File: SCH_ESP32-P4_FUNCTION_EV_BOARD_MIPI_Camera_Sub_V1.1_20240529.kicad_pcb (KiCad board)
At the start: 4 copper layers, 32 x 24 mm, 32 parts, among them J1 FPC_15P_R, J2 FPC_24P, Q3 DUAL_NMOS, SW1 NTC013-AT1J-A160T, U1 ME6211C18M5G-N, U2 ME6211C28M5G-N, Y1 24MHz

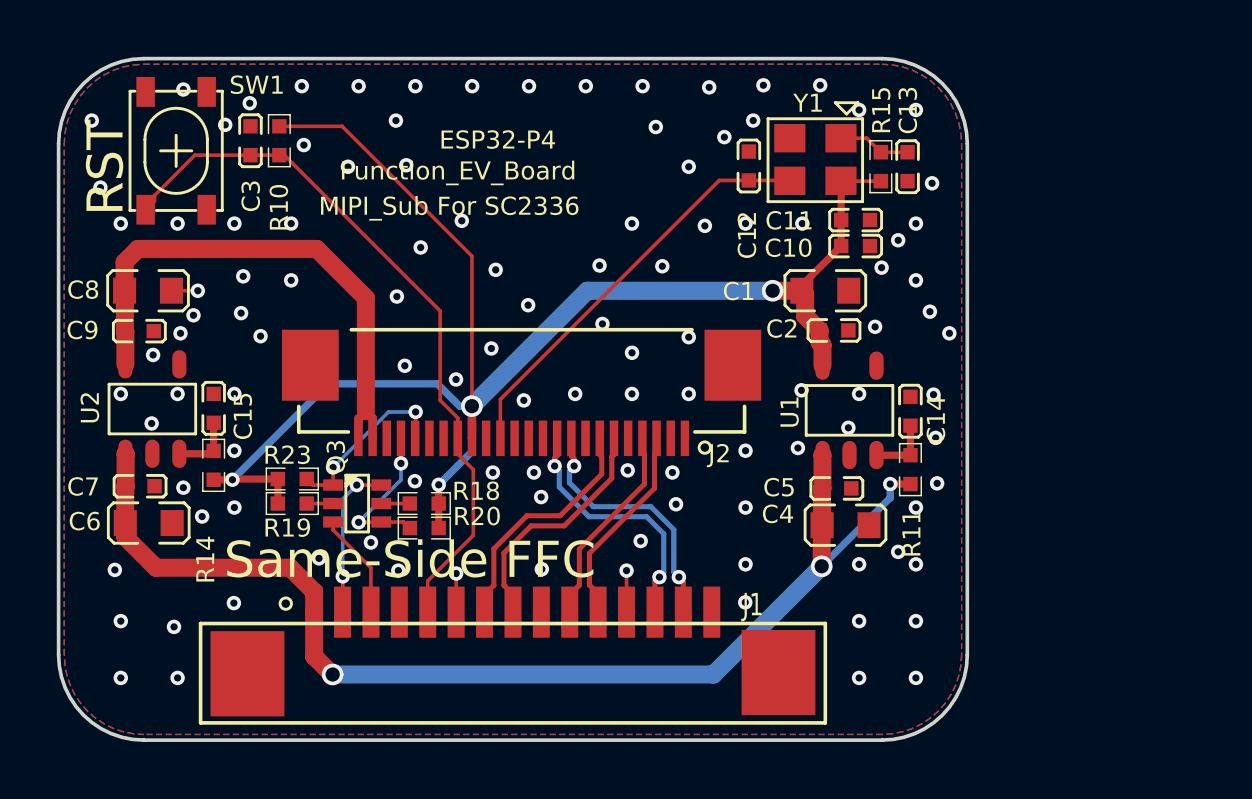
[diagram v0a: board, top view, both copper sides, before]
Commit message: pcb: lay out the SC035HGS adapter board
Update the PCB from the SC035HGS schematic and redo it: all of
Espressif's copper was removed and the parts re-placed and re-routed.
- 40 x 24 mm with R3 corners, 4 layers on JLC04161H-7628, 1.6 mm, ENIG
  (Board Setup minimums from pcb-fabrication-profile.json)
- J1 on the bottom edge, J2 on the top edge, J3 on the right edge
  opening outward (pin row 7.9 mm from the edge, per JAE SJ019575)
- In1 solid GND, In2 solid DOVDD_1V8; 3V3/DVDD_1V5/AVDD_2V8 as tracks
  in PWR_* netclasses
- MIPI CSI-2 pairs on the top layer, 100 ohm (0.2258/0.2032 mm), no
  vias, zero intra-pair skew; all vias 0.6/0.3 mm
- silkscreen text at 1.0/0.15 mm; MECH1/MECH2 dimension holders, the
  Allegro drill chart and off-board empty rule areas removed
- C12/C13/C14 (valued NC) set to DNP in schematic and PCB

DRC: 0 errors, 0 unconnected, 0 schematic parity issues; 86 silkscreen
warnings from Camera_Sub footprints whose silk extends past their
courtyards.

Co-Authored-By: Claude Opus 5.5 <noreply@anthropic.com>
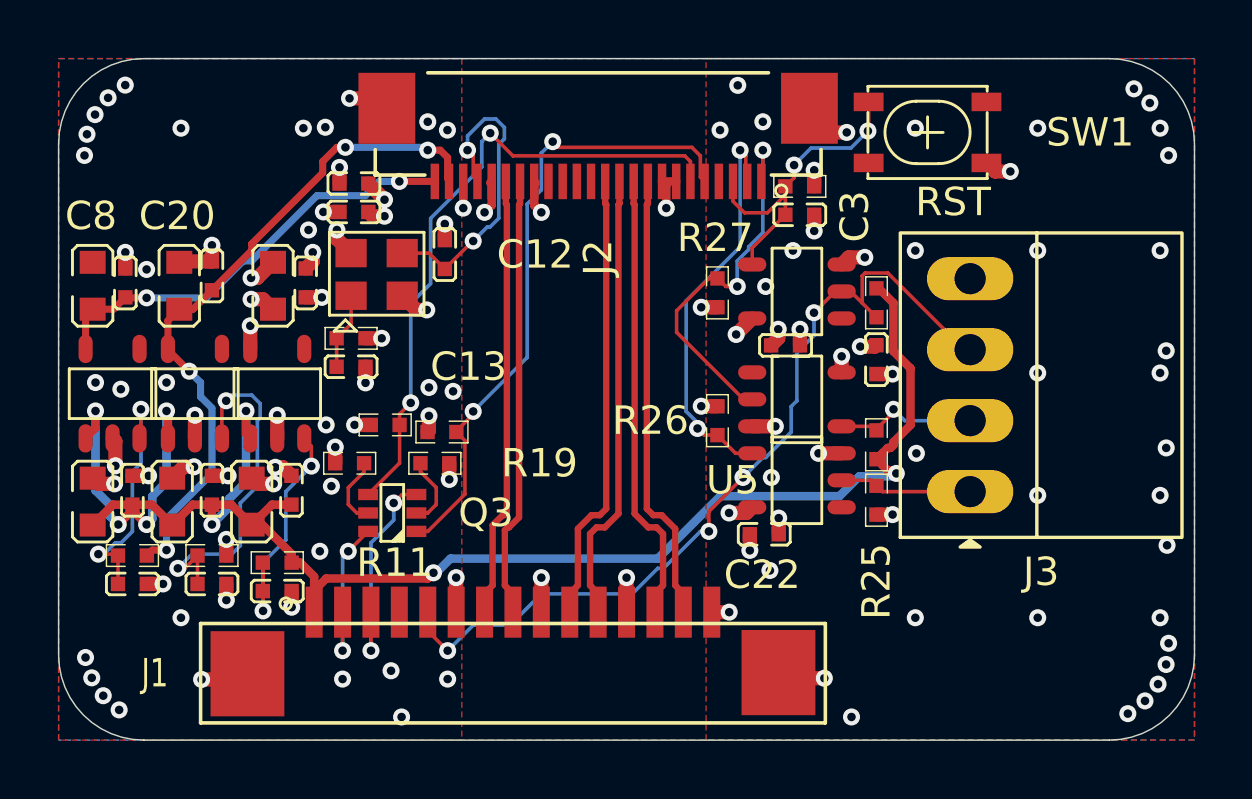
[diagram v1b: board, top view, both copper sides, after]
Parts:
- removed MECH1, MECH2: , 
- added C16: 10uF/6.3V(20%), Camera_Sub:C0603, F.Cu at (4.00, -8.40)
- added C17: 0.1uF/50V(10%), Camera_Sub:C0402, F.Cu at (5.40, -8.80)
- added C18: 0.1uF/50V(10%), Camera_Sub:C0402, F.Cu at (5.40, -5.50)
- added C19: 0.1uF/50V(10%), Camera_Sub:C0402, F.Cu at (5.40, -16.4)
- added C20: 10uF/6.3V(20%), Camera_Sub:C0603, F.Cu at (4.25, -16.0)
- added C21: 0.1uF/50V(10%), Camera_Sub:C0402, F.Cu at (25.6, -13.9)
- added C22: 0.1uF/50V(10%), Camera_Sub:C0402, F.Cu at (24.9, -7.25)
- added C23: 0.1uF/50V(10%), Camera_Sub:C0402, F.Cu at (28.8, -13.4)
- added J3: IL-G-4P-S3L2-SA, SC035HGS_Mod:JAE_IL-G-4P-S3L2-SA_1x04_P2.50mm_Horizontal, F.Cu at (32.1, -12.5)
- added R12: 10K(1%), Camera_Sub:R0402, F.Cu at (5.40, -6.50)
- added R24: 10K(1%), Camera_Sub:R0402, F.Cu at (28.8, -15.4)
- added R25: 100K(1%), Camera_Sub:R0402, F.Cu at (28.8, -8.45)
- added R26: 2.2K(1%), Camera_Sub:R0402, F.Cu at (23.2, -11.2)
- added R27: 100K(1%), Camera_Sub:R0402, F.Cu at (23.2, -15.8)
- added R28: 10K(1%), Camera_Sub:R0402, F.Cu at (28.8, -10.4)
- added U3: ME6211C15M5G-N, Camera_Sub:SOT23-5, F.Cu at (4.80, -12.2)
- added U4: SN74LVC1G07DBVR, Camera_Sub:SOT23-5, F.Cu at (26.0, -15.8)
- added U5: SN74LVC1G07DBVR, Camera_Sub:SOT23-5, F.Cu at (26.0, -9.15)
- added U6: SN74LVC1G07DBVR, Camera_Sub:SOT23-5, F.Cu at (26.0, -12.0)
- moved SW1 26.5 mm to (30.6, -21.4), turned to 180 degrees
- moved C14 23.2 mm to (7.70, -5.25), turned to 0 degrees
- moved R11 22.5 mm to (7.70, -6.25), turned to 0 degrees
- moved C4 20.9 mm to (6.80, -8.40), turned to 90 degrees
- moved C13 20.8 mm to (10.3, -13.2), turned to 0 degrees
- moved U1 20.2 mm to (7.70, -12.2)
- moved R15 19.6 mm to (10.3, -14.2), turned to 0 degrees
- moved C3 19.5 mm to (26.1, -18.5), turned to 0 degrees
- moved C1 19.5 mm to (7.55, -16.0), turned to 90 degrees
- moved C5 19.2 mm to (8.20, -8.80), turned to 90 degrees
- moved C2 18.7 mm to (8.70, -16.1), turned to 90 degrees
- moved R10 18.4 mm to (26.1, -19.5), turned to 0 degrees
- moved C10 17.8 mm to (10.4, -19.6)
- moved C11 17.7 mm to (10.4, -18.6)
- moved Y1 16.0 mm to (11.2, -16.4), turned to 0 degrees
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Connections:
- C12 pad 1: /XVCLK -> /MCLK
- C3 pad 1: /RESET -> /XSHUTDN
- J1 pad 5: /RESET -> /XSHUTDN_3V3
- J2 pad 1: unconnected-(J2-Pad1) -> /LED_STROBE
- J2 pad 11: unconnected-(J2-Pad11) -> /CSI_DATA1N
- J2 pad 12: unconnected-(J2-Pad12) -> /CSI_DATA1P
- J2 pad 13: GND -> unconnected-(J2-NC-Pad13)
- J2 pad 14: /XVCLK -> unconnected-(J2-NC-Pad14)
- J2 pad 15: GND -> unconnected-(J2-NC-Pad15)
- J2 pad 16: DOVDD_1V8 -> unconnected-(J2-NC-Pad16)
- J2 pad 17: /RESET -> GND
- J2 pad 18: unconnected-(J2-Pad18) -> /CSI_CLKN
- J2 pad 19: GND -> /CSI_CLKP
- J2 pad 2: unconnected-(J2-Pad2) -> /TRIG
- J2 pad 20: /SENSOR_SDA -> GND
- J2 pad 21: /SENSOR_SCL -> /MCLK
- J2 pad 22: GND -> DOVDD_1V8
- J2 pad 23: AVDD_2V8 -> DVDD_1V5
- J2 pad 3: /CSI_DATA1N -> /XSHUTDN
- J2 pad 4: /CSI_DATA1P -> unconnected-(J2-NC-Pad4)
- J2 pad 5: GND -> /SENSOR_SDA
- J2 pad 6: /CSI_CLKN -> /SENSOR_SCL
- J2 pad 7: /CSI_CLKP -> GND
- R10 pad 1: /RESET -> /XSHUTDN
- R14 pad 2: DOVDD_1V8 -> DVDD_1V5
- SW1 pad 3: /RESET -> /XSHUTDN
- Y1 pad 3: /XVCLK -> /MCLK
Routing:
- net DOVDD_1V8: track 55.3 -> 14.0 mm, vias 4 -> 21
- net GND: track 3.75 -> 38.2 mm, vias 113 -> 104
- net /XSHUTDN_3V3: track 0.00 -> 30.7 mm, vias 0 -> 4
- net /RESET: track 25.3 -> 0.00 mm
- net DVDD_1V5: track 0.00 -> 23.9 mm, vias 0 -> 4
- net 3V3: track 40.9 -> 61.1 mm, vias 3 -> 8
- net /SENSOR_SCL: track 5.47 -> 22.7 mm
- net /SENSOR_SDA: track 6.29 -> 22.5 mm
- net /XVCLK: track 14.8 -> 0.00 mm
- net /TRIG: track 0.00 -> 14.2 mm, vias 0 -> 2
- net /LED_STROBE: track 0.00 -> 13.4 mm, vias 0 -> 2
- net Net-(U3-EN): track 0.00 -> 12.5 mm, vias 0 -> 2
- net /XSHUTDN: track 0.00 -> 11.2 mm, vias 0 -> 2
- net /MCLK: track 0.00 -> 11.1 mm, vias 0 -> 2
- net /CSI_DATA1N: track 7.23 -> 15.9 mm
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- added copper zone on In2.Cu, net DOVDD_1V8
- removed copper zone on In2.Cu, net GND
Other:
- board size 32 x 24 mm -> 40 x 24 mm
- board text added: "MIPI_Sub For SC035HGS"
- board text removed: "0.254"
- board text removed: "0.5"
- board text removed: "126"
- board text removed: "4"
- board text removed: "ALL UNITS ARE IN MILLIMETERS"
- board text removed: "DRILL CHART: TOP to BOTTOM"
- board text removed: "FIGURE"
- board text removed: "MIPI_Sub For SC2336"
- board text removed: "PLATED"
- board text removed: "QTY"
- board text removed: "SIZE"

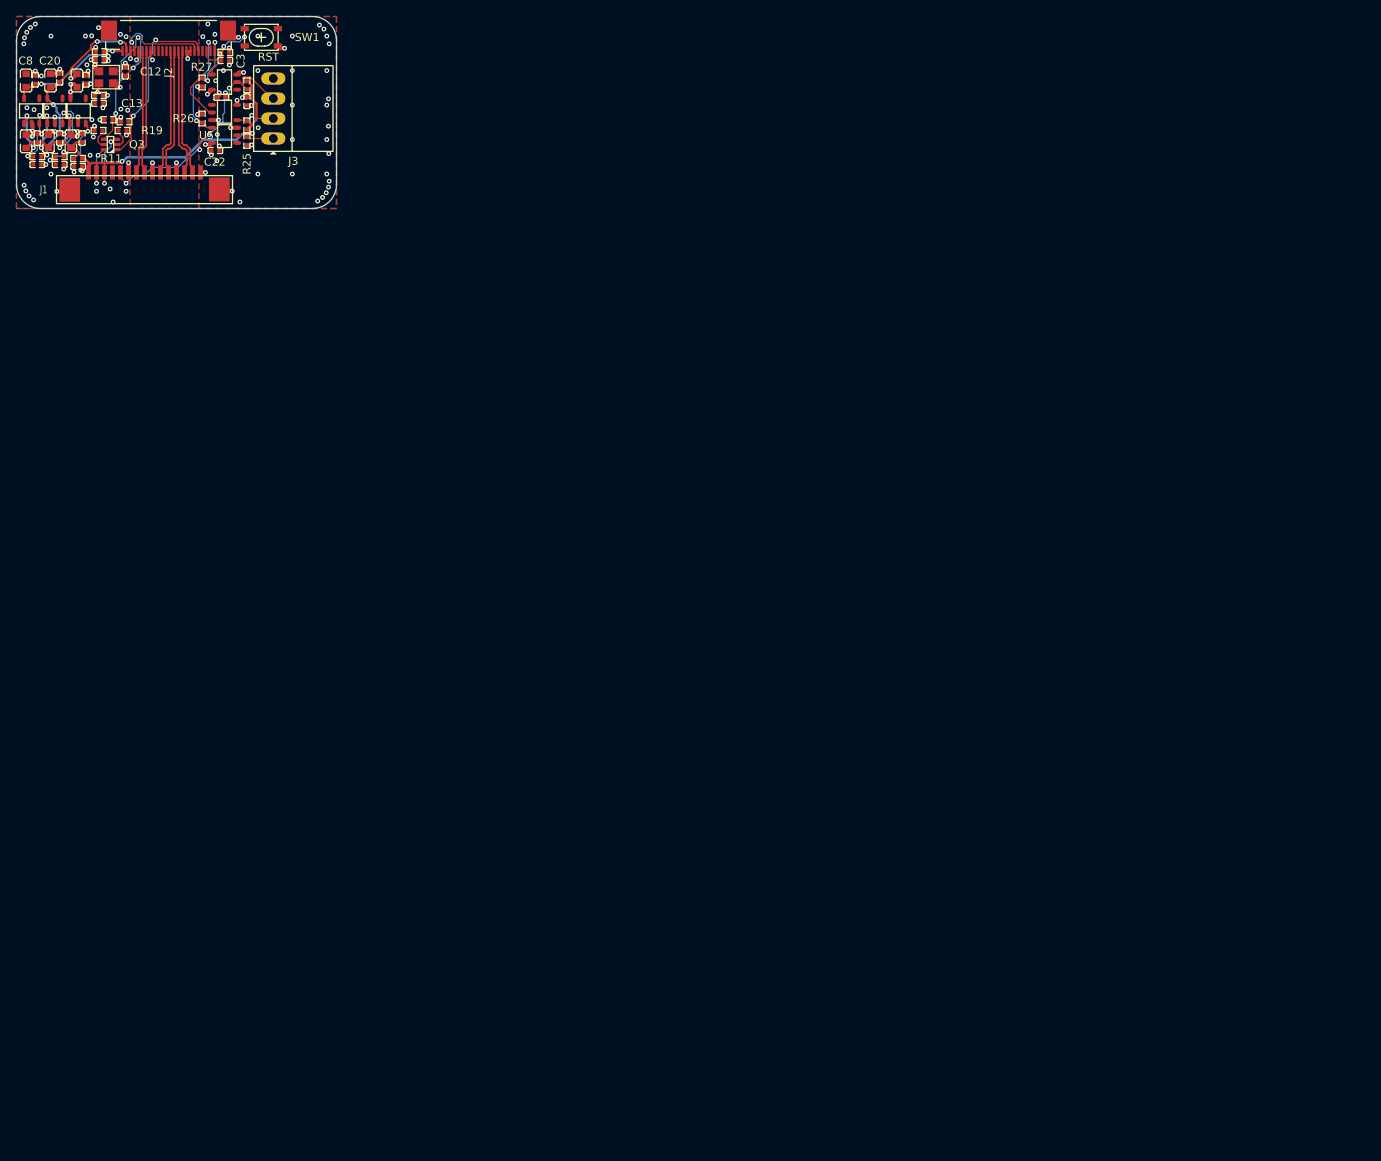
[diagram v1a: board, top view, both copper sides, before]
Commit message: pcb: tighten the MIPI routes, rework R24/R27 and clean up the silkscreen
- Re-route the three CSI pairs with a single 45-degree bend per turn
  (still top layer, no vias, zero intra-pair skew; pairs now within
  0.21 mm of each other).
- Rotate R24 and R27 and re-route XSHUTDN_3V3, 3V3 and LED_STROBE around
  them; move the GND via by R27 and extend the top GND pour so R27.1
  keeps its thermal spokes.
- Remove the board-level bottom silkscreen graphics (Espressif logo,
  WEEE/ESD/Pb-free/halogen-free marks) and the stale Route Keepin area.
- Move the whole board into the middle of the A4 drawing sheet.

ERC 0; DRC 0 errors, 0 unconnected, 0 parity, 87 silkscreen warnings.

Co-Authored-By: Claude Opus 5.5 <noreply@anthropic.com>
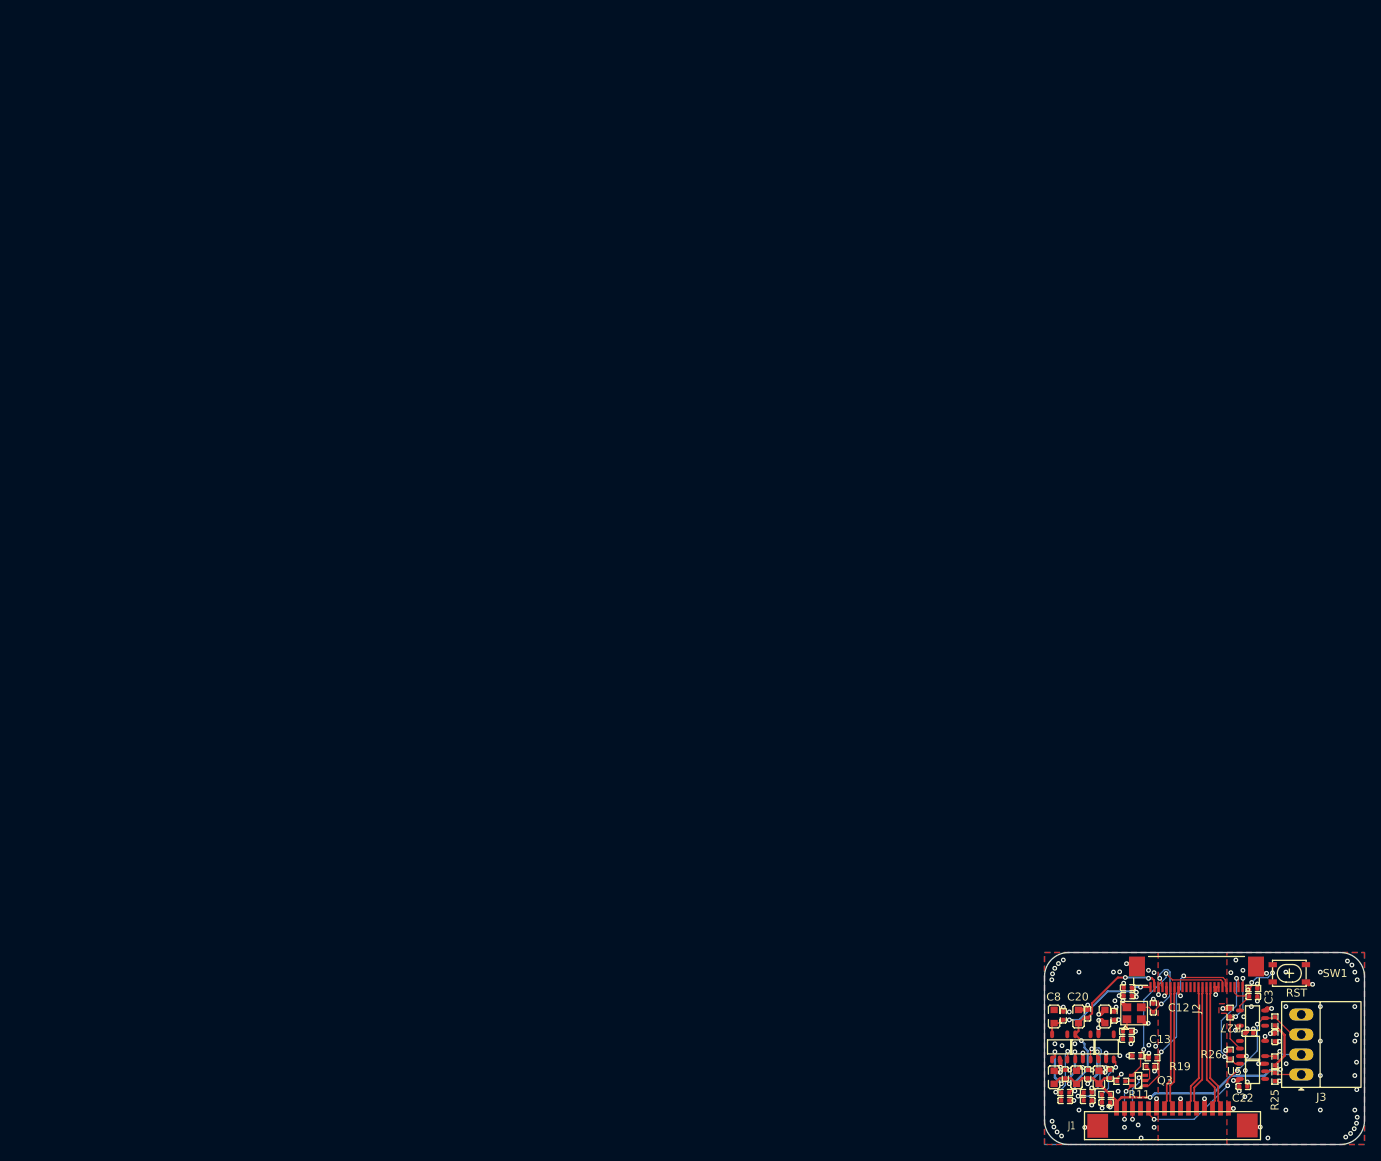
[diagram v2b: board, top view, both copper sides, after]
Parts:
- moved R18 174.6 mm to (138.1, 109.1)
- moved C1 173.8 mm to (136.1, 101.0)
- moved C10 173.8 mm to (138.9, 97.4)
- moved C11 173.8 mm to (138.9, 98.4)
- moved C12 173.8 mm to (142.1, 99.9)
- moved C13 173.8 mm to (138.8, 103.8)
- moved C14 173.8 mm to (136.2, 111.8)
- moved C15 173.8 mm to (131.1, 111.5)
- moved C16 173.8 mm to (132.5, 108.6)
- moved C17 173.8 mm to (133.9, 108.2)
- moved C18 173.8 mm to (133.9, 111.5)
- moved C19 173.8 mm to (133.9, 100.7)
- moved C2 173.8 mm to (137.2, 100.9)
- moved C20 173.8 mm to (132.8, 101.0)
- moved C21 173.8 mm to (154.1, 103.1)
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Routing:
- net /XSHUTDN_3V3: track 30.7 -> 28.7 mm
- net Net-(Q3-2G): track 2.50 -> 0.83 mm
- net /LED_STROBE: track 13.4 -> 11.8 mm
- net 3V3: track 61.1 -> 60.0 mm
- net DOVDD_1V8: track 14.0 -> 14.6 mm
- net GND: track 38.2 -> 38.5 mm, vias 104 -> 103
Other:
- board text removed: "HF"
